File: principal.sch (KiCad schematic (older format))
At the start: 31 parts, among them J1 TB_1X2, P2 CONN_02X01, Q1 2N7002, Q2 2N7002, Q3 2N7002, U1 24LC64, U2 LM2596, U3 NCP1117ST33T3G

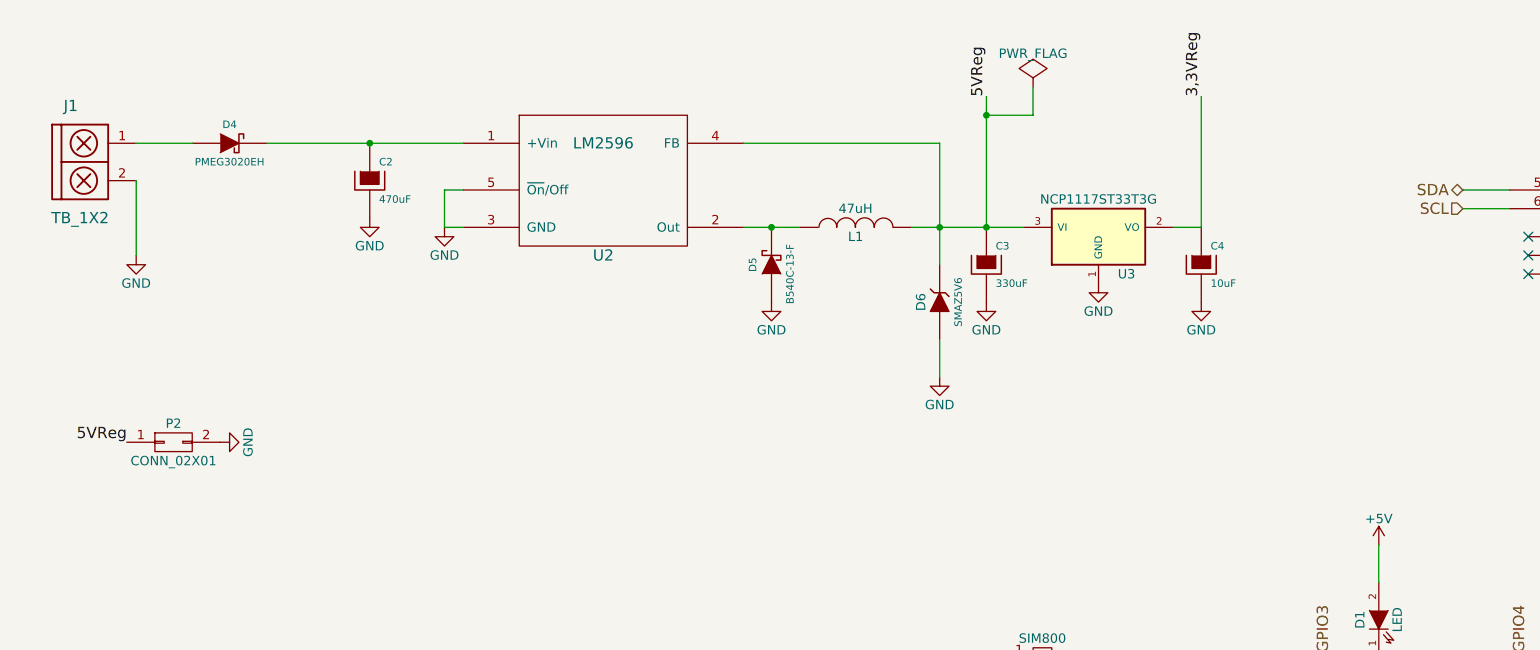
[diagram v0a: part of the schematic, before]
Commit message: agregada información de cada componente en el esquemático
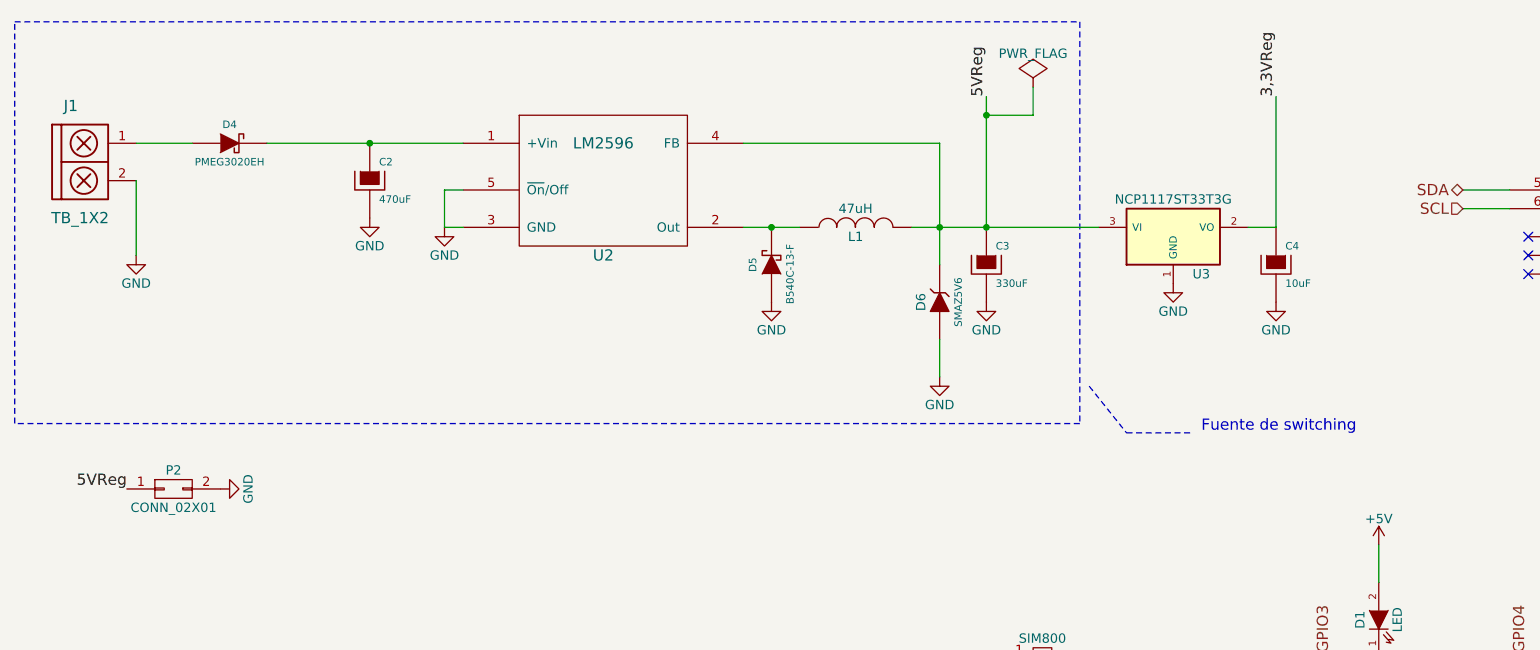
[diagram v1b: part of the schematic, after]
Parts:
- U1: Digikey# (none) -> 24LC64-I/SN-ND; Manf (none) -> Microchip Technology; Manf# (none) -> 24LC64-I/SN
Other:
- note added: "Fuente de switching"
- moved on the sheet: C4, P2, U3
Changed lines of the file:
@@
 EESchema Schematic File Version 2
-LIBS:falling_detector-rescue
-LIBS:power
-LIBS:device
-LIBS:transistors
-LIBS:conn
-LIBS:linear
-LIBS:regul
-LIBS:74xx
-LIBS:cmos4000
-LIBS:adc-dac
-LIBS:memory
-LIBS:xilinx
-LIBS:microcontrollers
-LIBS:dsp
-LIBS:microchip
-LIBS:analog_switches
-LIBS:motorola
-LIBS:texas
-LIBS:intel
-LIBS:audio
-LIBS:interface
-LIBS:digital-audio
-LIBS:philips
-LIBS:display
-LIBS:cypress
-LIBS:siliconi
-LIBS:opto
-LIBS:atmel
-LIBS:contrib
-LIBS:valves
-LIBS:ESP8266
-LIBS:lpc54102j512bd64
-LIBS:edu-ciaa-nxp
-LIBS:i2c
-LIBS:Misc_Poncho_Grande
+LIBS:falling_detector-cache
 LIBS:poncho_grande-cache
-LIBS:lm1117
-LIBS:lm2596
-LIBS:zener-rescue
-LIBS:tb_1x2
-LIBS:falling_detector-cache
+LIBS:trabajo_final-cache
 EELAYER 25 0
 EELAYER END
@@
 F 2 "Housings_SOIC:SOIC-8_3.9x4.9mm_Pitch1.27mm" H 9150 1900 60  0001 C CNN
 F 3 "" H 9150 1900 60  0000 C CNN
+F 4 "24LC64-I/SN-ND" H 9150 1900 60  0001 C CNN "Digikey#"
+F 5 "Microchip Technology" H 9150 1900 60  0001 C CNN "Manf"
+F 6 "24LC64-I/SN" H 9150 1900 60  0001 C CNN "Manf#"
 	1    9150 1900
 	1    0    0    -1
@@
 L CAPAPOL C4
 U 1 1 573B86BF
-P 6900 2050
-F 0 "C4" H 6950 2150 40  0000 L CNN
-F 1 "10uF" H 6950 1950 40  0000 L CNN
-F 2 "Capacitors_Tantalum_SMD:TantalC_SizeA_EIA-3216_HandSoldering" H 7000 1900 30  0001 C CNN
-F 3 "" H 6900 2050 300 0000 C CNN
-F 4 "Kemet" H 6900 2050 60  0001 C CNN "Manf"
-F 5 "T491A106K006AT7280" H 6900 2050 60  0001 C CNN "Manf#"
-F 6 "399-10116-1-ND" H 6900 2050 60  0001 C CNN "Digikey#"
-	1    6900 2050
+P 7300 2050
+F 0 "C4" H 7350 2150 40  0000 L CNN
+F 1 "10uF" H 7350 1950 40  0000 L CNN
+F 2 "Capacitors_Tantalum_SMD:TantalC_SizeA_EIA-3216_HandSoldering" H 7400 1900 30  0001 C CNN
+F 3 "" H 7300 2050 300 0000 C CNN
+F 4 "Kemet" H 7300 2050 60  0001 C CNN "Manf"
+F 5 "T491A106K006AT7280" H 7300 2050 60  0001 C CNN "Manf#"
+F 6 "399-10116-1-ND" H 7300 2050 60  0001 C CNN "Digikey#"
+	1    7300 2050
 	1    0    0    -1
 $EndComp
@@
 L NCP1117ST33T3G U3
 U 1 1 573B8DA4
-P 6350 1900
-F 0 "U3" H 6500 1700 50  0000 C CNN
-F 1 "NCP1117ST33T3G" H 6350 2100 50  0000 C CNN
-F 2 "TO_SOT_Packages_SMD:SOT-223" H 6350 1900 50  0001 C CNN
-F 3 "" H 6350 1900 50  0000 C CNN
-F 4 "ON Semiconductor" H 6350 1900 60  0001 C CNN "Manf"
-F 5 "NCP1117ST33T3G" H 6350 1900 60  0001 C CNN "Manf#"
-F 6 "NCP1117ST33T3GOSCT-ND" H 6350 1900 60  0001 C CNN "Digikey#"
-	1    6350 1900
+P 6750 1900
+F 0 "U3" H 6900 1700 50  0000 C CNN
+F 1 "NCP1117ST33T3G" H 6750 2100 50  0000 C CNN
+F 2 "TO_SOT_Packages_SMD:SOT-223" H 6750 1900 50  0001 C CNN
+F 3 "" H 6750 1900 50  0000 C CNN
+F 4 "ON Semiconductor" H 6750 1900 60  0001 C CNN "Manf"
+F 5 "NCP1117ST33T3G" H 6750 1900 60  0001 C CNN "Manf#"
+F 6 "NCP1117ST33T3GOSCT-ND" H 6750 1900 60  0001 C CNN "Digikey#"
+	1    6750 1900
 	1    0    0    -1
 $EndComp
@@
 L GND #PWR031
 U 1 1 573C3107
-P 6350 2150
-F 0 "#PWR031" H 6350 1900 50  0001 C CNN
-F 1 "GND" H 6350 2000 50  0000 C CNN
-F 2 "" H 6350 2150 50  0000 C CNN
-F 3 "" H 6350 2150 50  0000 C CNN
-	1    6350 2150
+P 6750 2150
+F 0 "#PWR031" H 6750 1900 50  0001 C CNN
+F 1 "GND" H 6750 2000 50  0000 C CNN
+F 2 "" H 6750 2150 50  0000 C CNN
+F 3 "" H 6750 2150 50  0000 C CNN
+	1    6750 2150
 	1    0    0    -1
 $EndComp
@@
 L GND #PWR032
 U 1 1 573C317E
-P 6900 2250
-F 0 "#PWR032" H 6900 2000 50  0001 C CNN
-F 1 "GND" H 6900 2100 50  0000 C CNN
-F 2 "" H 6900 2250 50  0000 C CNN
-F 3 "" H 6900 2250 50  0000 C CNN
-	1    6900 2250
+P 7300 2250
+F 0 "#PWR032" H 7300 2000 50  0001 C CNN
+F 1 "GND" H 7300 2100 50  0000 C CNN
+F 2 "" H 7300 2250 50  0000 C CNN
+F 3 "" H 7300 2250 50  0000 C CNN
+	1    7300 2250
 	1    0    0    -1
 $EndComp
@@
 L CONN_02X01 P2
 U 1 1 573C59E3
-P 1400 3000
-F 0 "P2" H 1400 3100 50  0000 C CNN
-F 1 "CONN_02X01" H 1400 2900 50  0000 C CNN
-F 2 "Pin_Headers:Pin_Header_Straight_2x01" H 1400 1800 50  0001 C CNN
-F 3 "" H 1400 1800 50  0000 C CNN
-F 4 "TE Connectivity AMP Connectors" H 1400 3000 60  0001 C CNN "Manf"
-F 5 "640456-2" H 1400 3000 60  0001 C CNN "Manf#"
-F 6 "A1921-ND" H 1400 3000 60  0001 C CNN "Digikey#"
-	1    1400 3000
+P 1400 3250
+F 0 "P2" H 1400 3350 50  0000 C CNN
+F 1 "CONN_02X01" H 1400 3150 50  0000 C CNN
+F 2 "Pin_Headers:Pin_Header_Straight_2x01" H 1400 2050 50  0001 C CNN
+F 3 "" H 1400 2050 50  0000 C CNN
+F 4 "TE Connectivity AMP Connectors" H 1400 3250 60  0001 C CNN "Manf"
+F 5 "640456-2" H 1400 3250 60  0001 C CNN "Manf#"
+F 6 "A1921-ND" H 1400 3250 60  0001 C CNN "Digikey#"
+	1    1400 3250
 	1    0    0    -1
 $EndComp
@@
 L GND #PWR034
 U 1 1 573C5A9C
-P 1650 3000
-F 0 "#PWR034" H 1650 2750 50  0001 C CNN
-F 1 "GND" H 1650 2850 50  0000 C CNN
-F 2 "" H 1650 3000 50  0000 C CNN
-F 3 "" H 1650 3000 50  0000 C CNN
-	1    1650 3000
+P 1650 3250
+F 0 "#PWR034" H 1650 3000 50  0001 C CNN
+F 1 "GND" H 1650 3100 50  0000 C CNN
+F 2 "" H 1650 3250 50  0000 C CNN
+F 3 "" H 1650 3250 50  0000 C CNN
+	1    1650 3250
 	0    -1   -1   0
-$EndComp
-$Comp
-L PWR_FLAG #FLG035
-U 1 1 573C7156
-P 6000 1100
-F 0 "#FLG035" H 6000 1195 50  0001 C CNN
-F 1 "PWR_FLAG" H 6000 1280 50  0000 C CNN
-F 2 "" H 6000 1100 50  0000 C CNN
-F 3 "" H 6000 1100 50  0000 C CNN
-	1    6000 1100
-	1    0    0    -1
 $EndComp
 Text Label 5750 1150 1    60   ~ 0
 5VReg
-Text Label 6900 1150 1    60   ~ 0
+Text Label 7300 1150 1    60   ~ 0
 3,3VReg
 Wire Wire Line
@@
 Connection ~ 4600 1850
 Wire Wire Line
-	5350 1850 5950 1850
+	5350 1850 6350 1850
 Connection ~ 5500 1850
 Connection ~ 5750 1850
 Wire Wire Line
-	6750 1850 6900 1850
+	7150 1850 7300 1850
 Wire Wire Line
 	5750 1850 5750 1150
 Wire Wire Line
-	5750 1250 6000 1250
-Wire Wire Line
-	6000 1250 6000 1100
-Connection ~ 5750 1250
-Wire Wire Line
-	6900 1850 6900 1150
-Text Label 1150 3000 2    60   ~ 0
+	7300 1850 7300 1150
+Text Label 1150 3250 2    60   ~ 0
 5VReg
 Wire Wire Line
@@
 	1    0    0    -1
 $EndComp
+Wire Notes Line
+	6250 750  6250 2900
+Wire Notes Line
+	6250 2900 550  2900
+Wire Notes Line
+	550  2900 550  750
+Wire Notes Line
+	550  750  6250 750
+Wire Notes Line
+	6300 2700 6500 2950
+Wire Notes Line
+	6500 2950 6850 2950
+Text Notes 6900 2950 0    60   ~ 0
+Fuente de switching
+Connection ~ 5750 1250
+Wire Wire Line
+	5750 1250 6000 1250
+Wire Wire Line
+	6000 1250 6000 1100
+$Comp
+L PWR_FLAG #FLG035
+U 1 1 573C7156
+P 6000 1100
+F 0 "#FLG035" H 6000 1195 50  0001 C CNN
+F 1 "PWR_FLAG" H 6000 1280 50  0000 C CNN
+F 2 "" H 6000 1100 50  0000 C CNN
+F 3 "" H 6000 1100 50  0000 C CNN
+	1    6000 1100
+	1    0    0    -1
+$EndComp

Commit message: cambio de pc
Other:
- note added: "Fuente de switching 5 V"
- note added: "LEDs indicadores de estado"
- note added: "Memoria EEPROM"
- note added: "Módulo Acelerómetro"
- note added: "Módulo GSM"
- note added: "Módulo WiFi"
- note added: "Regulador lineal 3,3 V"
- note removed: "Fuente de switching"
- moved on the sheet: D1, D2, D3, P2, Q1, Q2, Q3, R1, R2, R3, R4, R5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

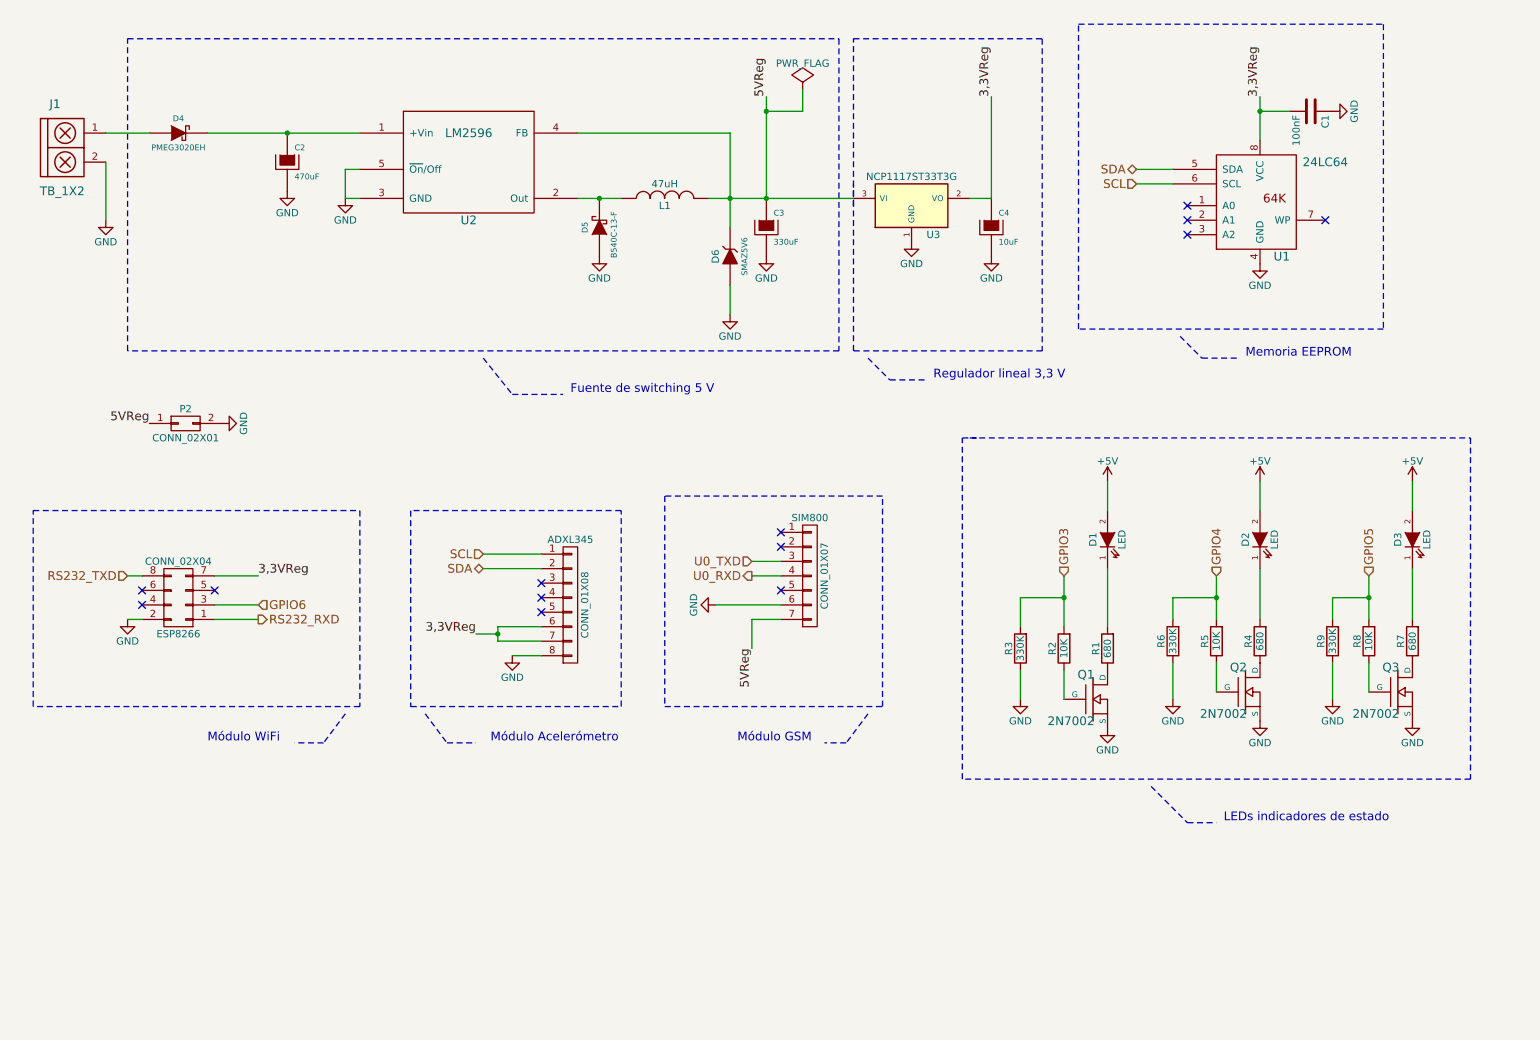
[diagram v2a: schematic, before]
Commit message: agregado buzzer y medidor de batería
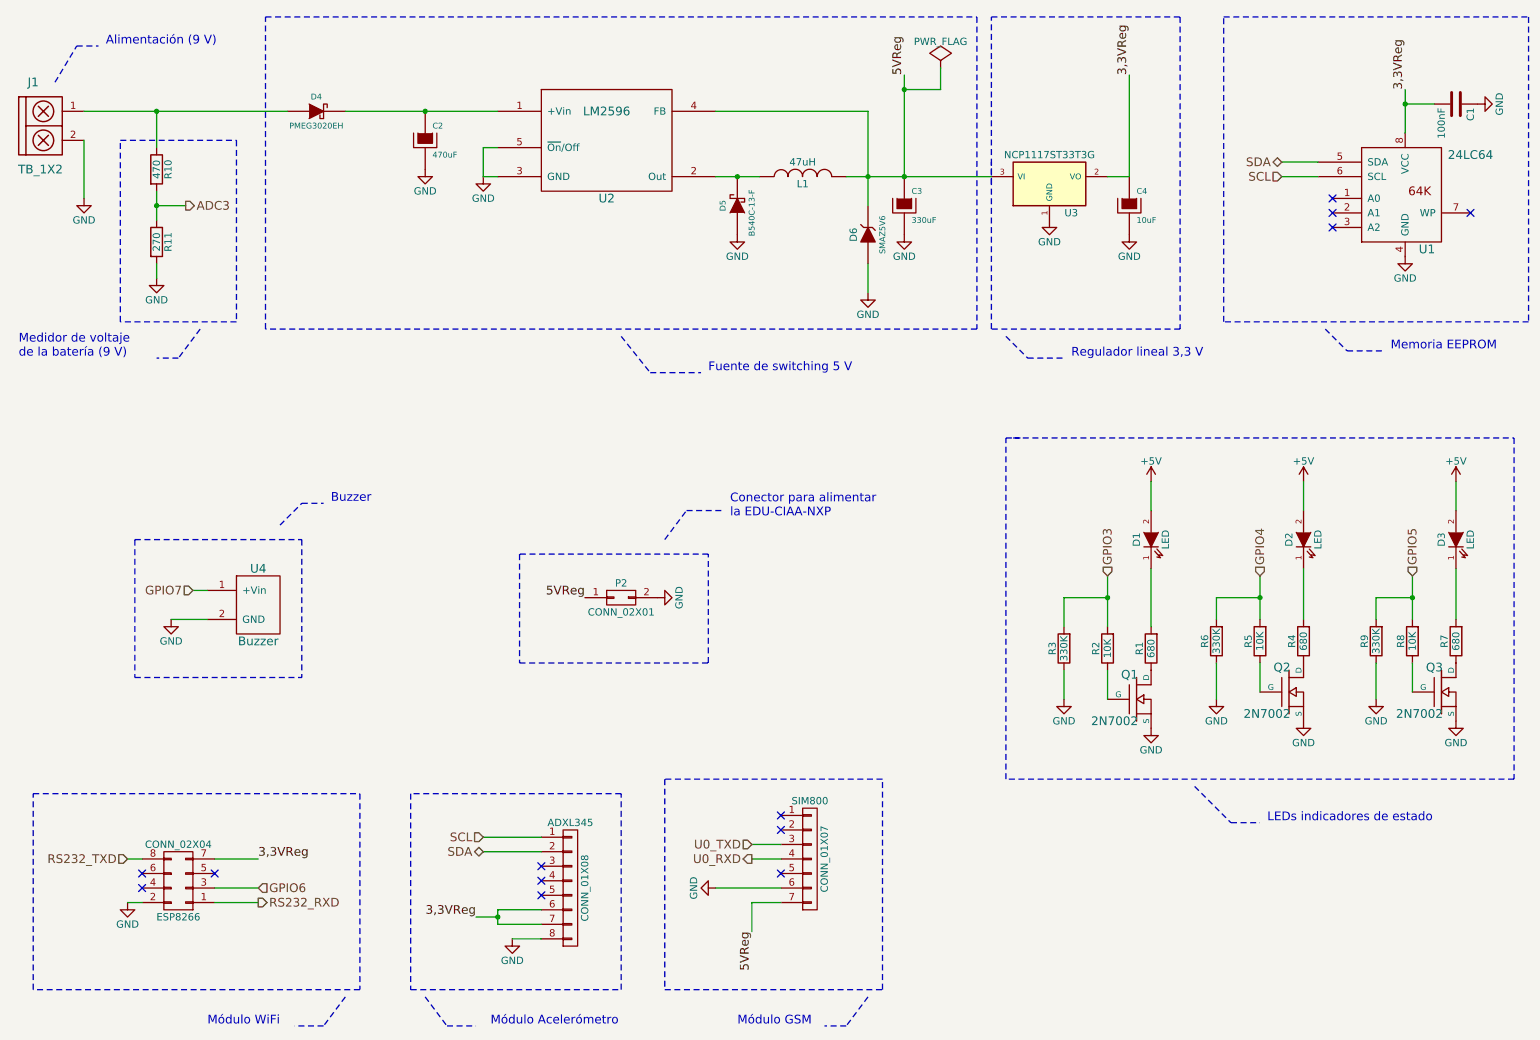
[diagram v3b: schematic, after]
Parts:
- added R10: 470, symbol R
- added R11: 270, symbol R
- added U4: Buzzer, symbol Buzzer
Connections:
- net GND: now also R11.2, U4.2 (GND)
- net at D4.1 (A), J1.1: now also R10.1
- new net ADC3: R10.2, R11.1
- new net GPIO7: U4.1 (+Vin)
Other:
- note added: "Alimentación (9 V)"
- note added: "Buzzer"
- note added: "Conector para alimentar\nla EDU-CIAA-NXP"
- note added: "Medidor de voltaje\nde la batería (9 V)"
- moved on the sheet: ADXL345, C1, C2, C3, C4, D1, D2, D3, D4, D5, D6, ESP8266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

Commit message: cambio de pc
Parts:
- R10, R11: footprint (none) -> Resistors_SMD:R_0805_HandSoldering
- U4: footprint (none) -> mod:Buzzer_12x9.5RM7.6; Manf (none) -> Value; Manf# (none) -> Value
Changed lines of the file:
@@
 F 0 "R10" V 1630 1650 50  0000 C CNN
 F 1 "470" V 1550 1650 50  0000 C CNN
-F 2 "" V 1480 1650 50  0001 C CNN
+F 2 "Resistors_SMD:R_0805_HandSoldering" V 1480 1650 50  0001 C CNN
 F 3 "" H 1550 1650 50  0000 C CNN
 	1    1550 1650
@@
 F 0 "R11" V 1630 2150 50  0000 C CNN
 F 1 "270" V 1550 2150 50  0000 C CNN
-F 2 "" V 1480 2150 50  0001 C CNN
+F 2 "Resistors_SMD:R_0805_HandSoldering" V 1480 2150 50  0001 C CNN
 F 3 "" H 1550 2150 50  0000 C CNN
 	1    1550 2150
@@
 F 0 "U4" H 2250 5000 60  0000 C CNN
 F 1 "Buzzer" H 2250 4500 60  0000 C CNN
-F 2 "" H 2250 4700 60  0000 C CNN
+F 2 "mod:Buzzer_12x9.5RM7.6" H 2250 4700 60  0001 C CNN
 F 3 "" H 2250 4700 60  0000 C CNN
+F 4 "Value" H 2250 4700 60  0001 C CNN "Manf"
+F 5 "Value" H 2250 4700 60  0001 C CNN "Manf#"
 	1    2250 4700
 	1    0    0    -1
@@
 Wire Wire Line
 	1800 4550 1900 4550
+$Comp
+L GNDA #PWR?
+U 1 1 578FAC51
+P 1800 2350
+F 0 "#PWR?" H 1800 2100 50  0001 C CNN
+F 1 "GNDA" H 1800 2200 50  0000 C CNN
+F 2 "" H 1800 2350 50  0000 C CNN
+F 3 "" H 1800 2350 50  0000 C CNN
+	1    1800 2350
+	0    -1   -1   0
+$EndComp
+Wire Wire Line
+	1800 2350 1550 2350
+Connection ~ 1550 2350
 $EndSCHEMATC

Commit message: merge resuelta
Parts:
- added Q4: 2N7002, TO_SOT_Packages_SMD:SOT-23_Handsoldering, symbol MOSFET_N-RESCUE-falling_detector
- added R12: 10K, Resistors_SMD:R_0805_HandSoldering, symbol R
- added R13: 330K, Resistors_SMD:R_0805_HandSoldering, symbol R
- added R14: 680, Resistors_SMD:R_0805_HandSoldering, symbol R
- R10: value 470 -> 470K; footprint Resistors_SMD:R_0805_HandSoldering -> (none)
- R11: value 270 -> 270K; footprint Resistors_SMD:R_0805_HandSoldering -> (none)
- U4: footprint mod:Buzzer_12x9.5RM7.6 -> (none); Manf Value -> (none); Manf# Value -> (none)
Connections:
- net +5V: now also U4.1 (+Vin)
- net GND: now also Q4.2 (S), R13.2; no longer U4.2 (GND)
- net GPIO3: now also R5.2, R6.2; no longer R2.2, R3.2
- net GPIO4: now also R2.2, R3.2; no longer R5.2, R6.2
- net GPIO7: now also R12.1, R13.1; no longer U4.1 (+Vin)
- new net: R14.1, U4.2 (GND)
- new net: Q4.1 (G), R12.2
- new net: Q4.3 (D), R14.2
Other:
- moved on the sheet: Q1, Q2, Q3, U4

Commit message: ruteo casi terminado
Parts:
- added C5: 100nF, Capacitors_SMD:C_0805_HandSoldering, symbol C
- R10: footprint (none) -> Resistors_SMD:R_0805_HandSoldering; Digikey# (none) -> RMCF0805JT470KCT-ND; Manf (none) -> Stackpole Electronics Inc.; Manf# (none) -> RMCF0805JT470K
- R11: footprint (none) -> Resistors_SMD:R_0805_HandSoldering; Digikey# (none) -> RMCF0805JT270KDKR-ND; Manf (none) -> Stackpole Electronics Inc.; Manf# (none) -> RMCF0805JT270K
- U4: footprint (none) -> footprints:Buzzer_12x9.5RM7.6
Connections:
- net +5V is gone; now on net 5VReg: D1.2 (A), D2.2 (A), D3.2 (A), U4.1 (+Vin)
- net ADC3: now also C5.2
- net GND: now also C5.1
- net RS232_RXD: now also SIM800.4 (P4); no longer ESP8266.1 (P1)
- net RS232_TXD: now also SIM800.3 (P3); no longer ESP8266.8 (P8)
- net U0_RXD: now also ESP8266.1 (P1); no longer SIM800.4 (P4)
- net U0_TXD: now also ESP8266.8 (P8); no longer SIM800.3 (P3)
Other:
- moved on the sheet: D5
